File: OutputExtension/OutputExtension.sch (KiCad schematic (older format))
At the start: 18 parts, among them P1 CONN_01X04, P2 CONN_01X04, P3 CONN_01X04, P4 CONN_01X08, P5 CONN_01X08, U1 PCF8574

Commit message: Output extension looks good. Diodes still missing
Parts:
- added JP1: A0, Connector_PinHeader_2.54mm:PinHeader_1x03_P2.54mm_Vertical, symbol Device:Jumper_NC_Dual
- added JP2: A1, Connector_PinHeader_2.54mm:PinHeader_1x03_P2.54mm_Vertical, symbol Device:Jumper_NC_Dual
- added JP3: A2, Connector_PinHeader_2.54mm:PinHeader_1x03_P2.54mm_Vertical, symbol Device:Jumper_NC_Dual
- C1, C2: value 100n -> 1u; footprint Capacitors_ThroughHole:C_Disc_D12_P7.75 -> Capacitor_SMD:C_0805_2012Metric; symbol C -> OutputExtension-rescue:C-OutputExtension-rescue
- C3: value 330n -> 1u; footprint Capacitors_SMD:C_0805_HandSoldering -> Capacitor_SMD:C_0805_2012Metric; symbol C -> OutputExtension-rescue:C-OutputExtension-rescue
- C4: value 100n -> 1u; footprint Capacitors_SMD:C_0805_HandSoldering -> Capacitor_SMD:C_0805_2012Metric; symbol C -> OutputExtension-rescue:C-OutputExtension-rescue
- C5, C6: symbol CP -> OutputExtension-rescue:CP-OutputExtension-rescue
- D1, D2: footprint LEDs:LED-0805 -> LED_SMD:LED_0805_2012Metric; symbol LED -> OutputExtension-rescue:LED-OutputExtension-rescue
- F1, F2: symbol FUSE -> OutputExtension-rescue:FUSE-OutputExtension-rescue
- P1: footprint Pin_Headers:Pin_Header_Straight_1x04 -> Connector_PinHeader_2.54mm:PinHeader_1x04_P2.54mm_Vertical; symbol CONN_01X04 -> OutputExtension-rescue:CONN_01X04-OutputExtension-rescue
- P2: renamed from P3; footprint Pin_Headers:Pin_Header_Straight_1x04 -> Connector_PinHeader_2.54mm:PinHeader_1x04_P2.54mm_Vertical; symbol CONN_01X04 -> OutputExtension-rescue:CONN_01X04-OutputExtension-rescue
- P3: renamed from P2; footprint my_foots:HT396_4 -> myStuff:HT396_4; symbol CONN_01X04 -> OutputExtension-rescue:CONN_01X04-OutputExtension-rescue
- P4, P5: footprint my_foots:HT396_8 -> myStuff:HT396_8; symbol CONN_01X08 -> OutputExtension-rescue:CONN_01X08-OutputExtension-rescue
- R1, R2: symbol R -> OutputExtension-rescue:R-OutputExtension-rescue
- U1: symbol PCA9534 -> OutputExtension-rescue:PCA9534-OutputExtension-rescue
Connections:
- net +5V: now also JP1.3, JP2.3, JP3.3
- net GND: now also JP1.1, JP2.1, JP3.1; no longer U1.1 (A0), U1.2 (A1), U1.3 (A2)
- net powerChannel0/Drain renamed powerChannel0/DRAIN
- net powerChannel1/Drain renamed powerChannel1/DRAIN
- net powerChannel2/Drain renamed powerChannel2/DRAIN
- net powerChannel3/Drain renamed powerChannel3/DRAIN
- net powerChannel4/Drain renamed powerChannel4/DRAIN
- net powerChannel5/Drain renamed powerChannel5/DRAIN
- net powerChannel6/Drain renamed powerChannel6/DRAIN
- net powerChannel7/Drain renamed powerChannel7/DRAIN
- new net A0: JP1.2, U1.1 (A0)
- new net A1: JP2.2, U1.2 (A1)
- new net A2: JP3.2, U1.3 (A2)
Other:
- moved on the sheet: C1, C2, C4, P1, P2

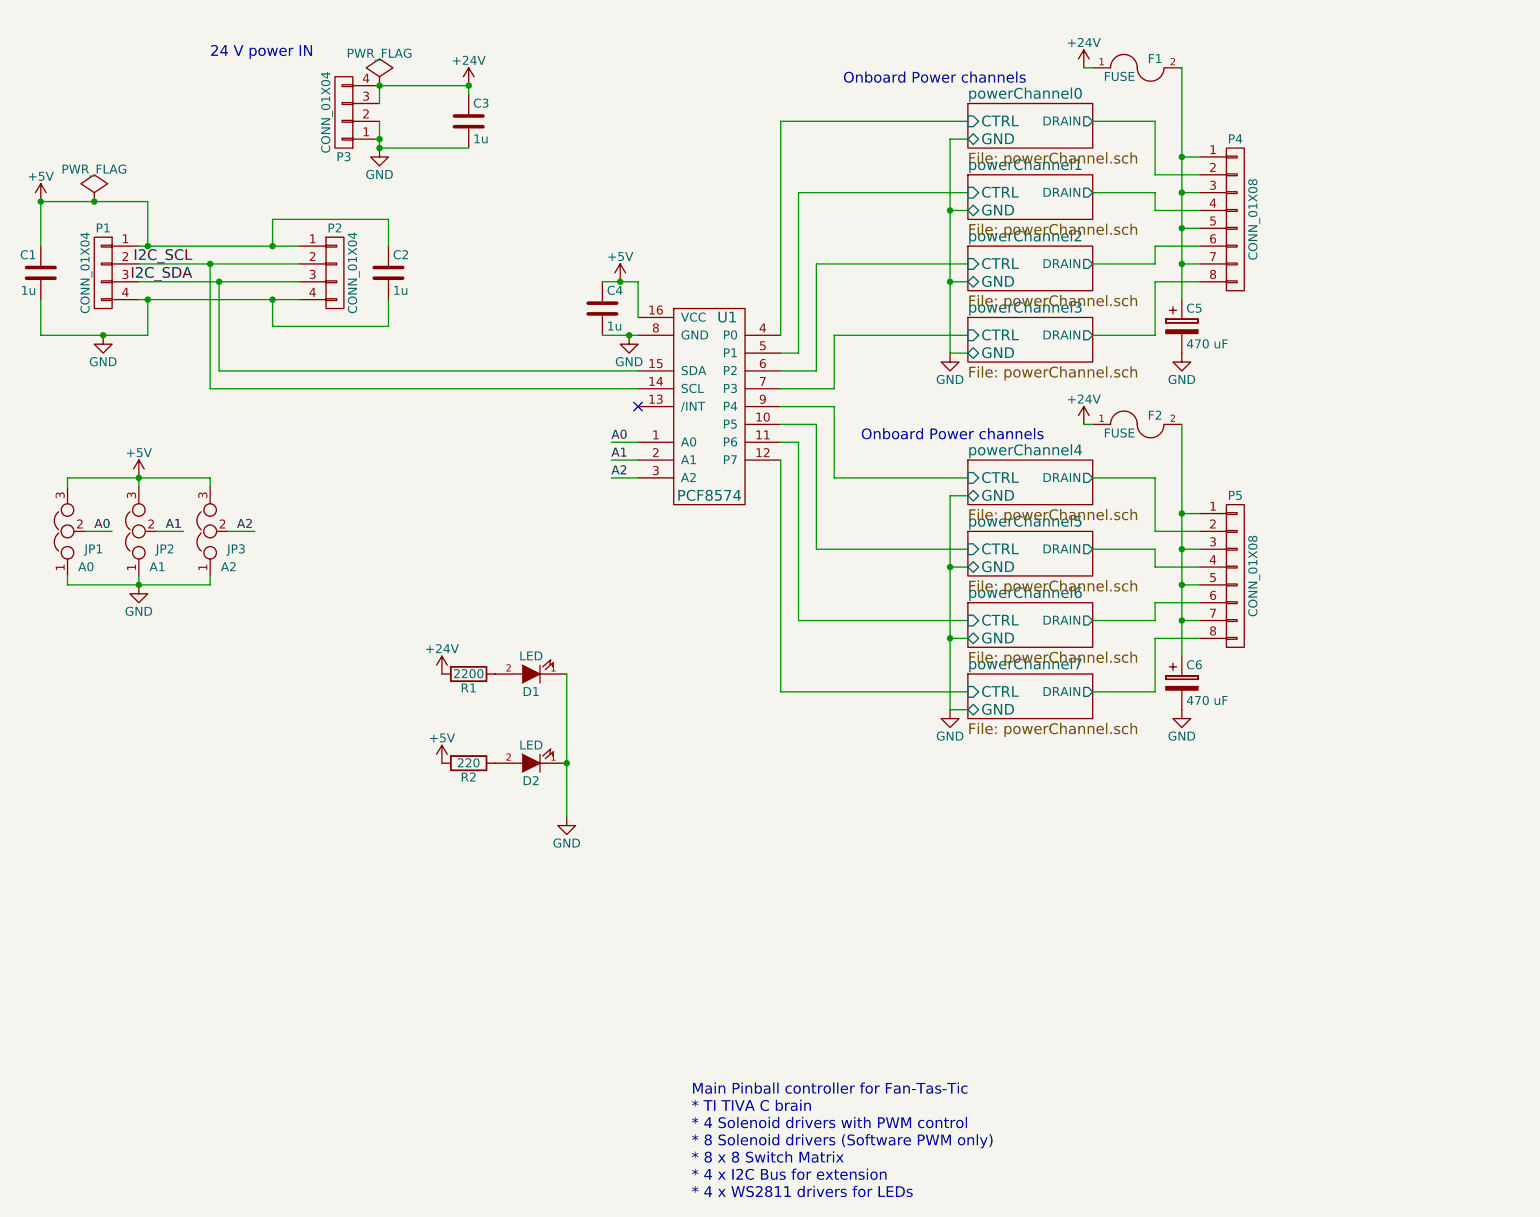
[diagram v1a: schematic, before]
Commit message: Add diodes
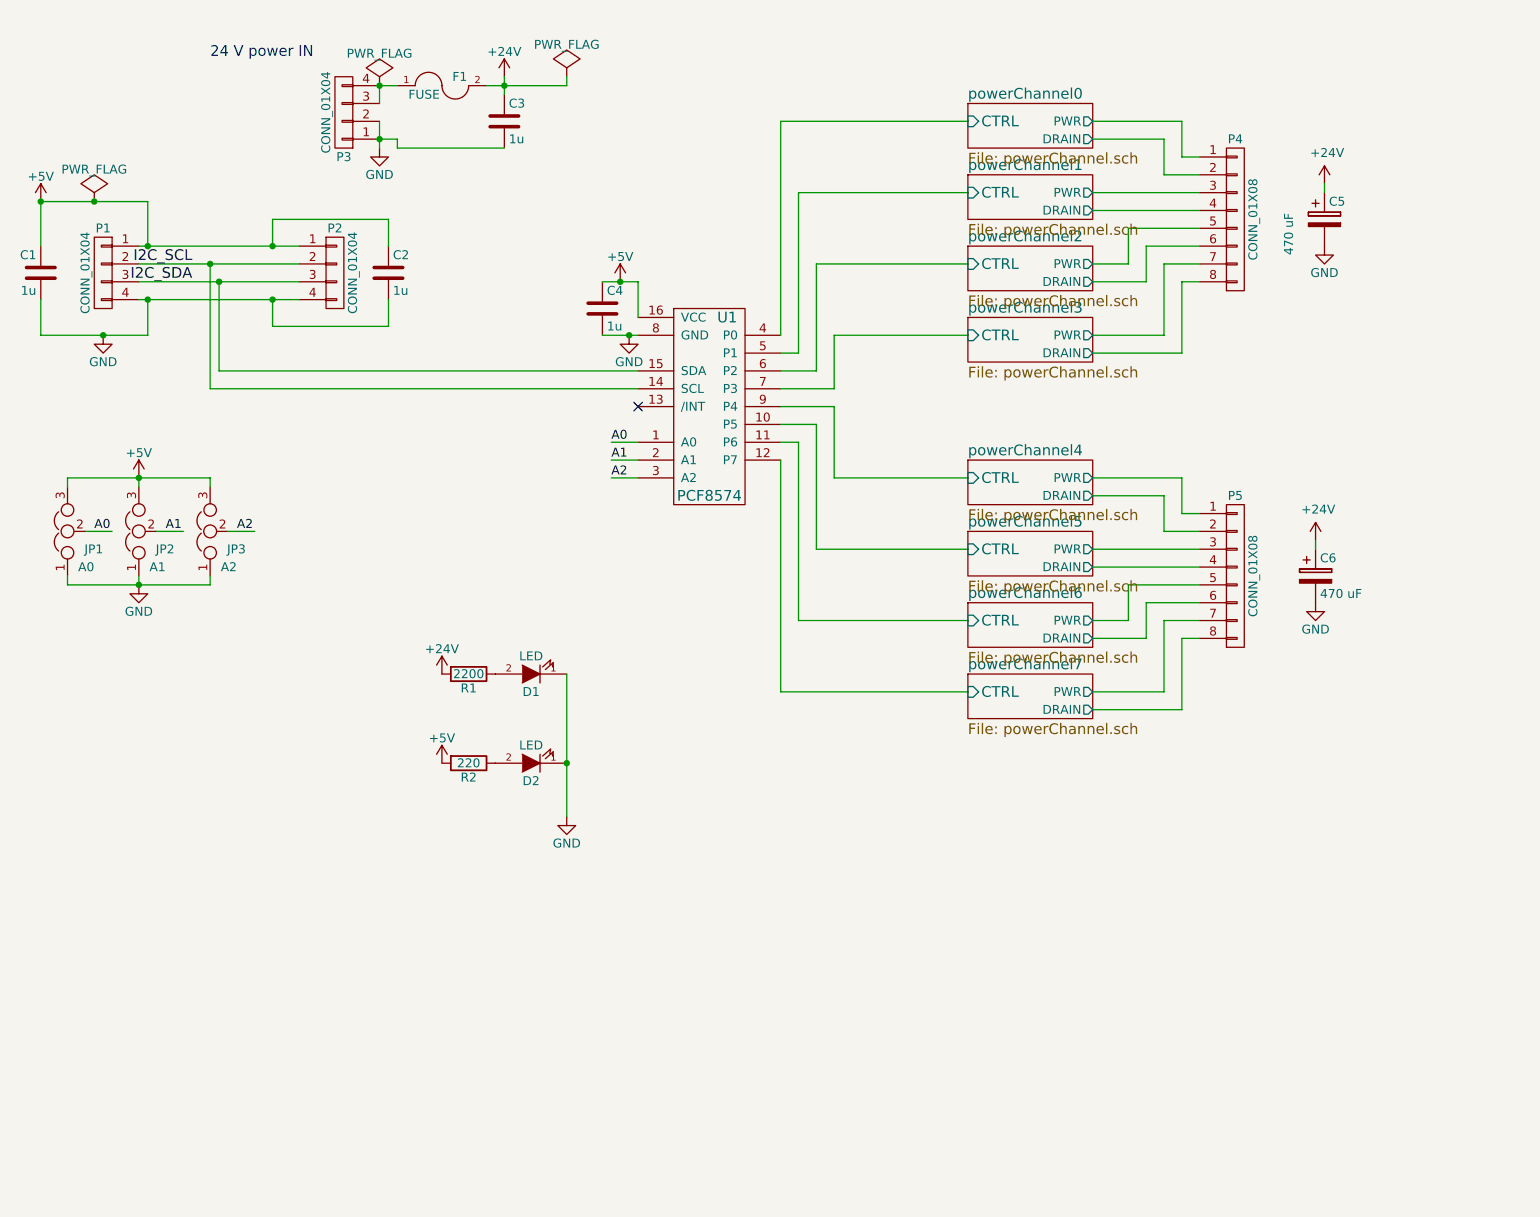
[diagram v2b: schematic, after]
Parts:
- removed F2: FUSE, Fuse_Holders_and_Fuses:Fuseholder5x20_horiz_open_lateral_Type-II, symbol OutputExtension-rescue:FUSE-OutputExtension-rescue
- R1, R2: footprint Resistors_SMD:R_0805_HandSoldering -> Resistor_SMD:R_0805_2012Metric
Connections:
- net +24V: now also C5.1, C6.1, F1.2; no longer F1.1, P3.3 (P3), P3.4 (P4)
- new net: F1.1, P3.3 (P3), P3.4 (P4)
- new net powerChannel0/PWR: P4.1 (P1)
- new net powerChannel1/PWR: P4.3 (P3)
- new net powerChannel2/PWR: P4.5 (P5)
- new net powerChannel3/PWR: P4.7 (P7)
- new net powerChannel4/PWR: P5.1 (P1)
- new net powerChannel5/PWR: P5.3 (P3)
- new net powerChannel6/PWR: P5.5 (P5)
- new net powerChannel7/PWR: P5.7 (P7)
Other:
- note removed: "Main Pinball controller for Fan-Tas-Tic\n* TI TIVA C brain\n* 4 Solenoid drivers with PWM control\n* 8 Solenoid drivers (Software PWM only)\n* 8 x 8 Switch Matrix\n* 4 x I2C Bus for extension\n* 4 x WS2811 drivers for LEDs\n"
- note removed: "Onboard Power channels"
- moved on the sheet: C3, C5, C6, F1

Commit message: Output extension ready for fab
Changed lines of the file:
@@
 $EndComp
 $Sheet
-S 6150 1150 700  250
+S 5950 1150 700  250
 U 568473CE
 F0 "powerChannel0" 60
 F1 "powerChannel.sch" 60
-F2 "CTRL" I L 6150 1250 60
-F3 "DRAIN" O R 6850 1350 50
-F4 "PWR" O R 6850 1250 50
+F2 "CTRL" I L 5950 1250 60
+F3 "DRAIN" O R 6650 1350 50
+F4 "PWR" O R 6650 1250 50
 $EndSheet
 $Comp
@@
 	7350 1450 7450 1450
 Wire Wire Line
-	5200 1650 6150 1650
-Wire Wire Line
-	5400 2450 6150 2450
-Wire Wire Line
-	5100 1250 6150 1250
-Wire Wire Line
-	5300 2050 6150 2050
+	5200 1650 5950 1650
+Wire Wire Line
+	5400 2450 5950 2450
+Wire Wire Line
+	5100 1250 5950 1250
+Wire Wire Line
+	5300 2050 5950 2050
 Wire Wire Line
 	7350 3450 7450 3450
 Wire Wire Line
-	5300 3650 6150 3650
-Wire Wire Line
-	5100 4450 6150 4450
-Wire Wire Line
-	5400 3250 6150 3250
-Wire Wire Line
-	5200 4050 6150 4050
+	5300 3650 5950 3650
+Wire Wire Line
+	5100 4450 5950 4450
+Wire Wire Line
+	5400 3250 5950 3250
+Wire Wire Line
+	5200 4050 5950 4050
 Wire Wire Line
 	5100 2450 5100 1250
@@
 	1950 2150 2400 2150
 $Sheet
-S 6150 2350 700  250
+S 5950 2350 700  250
 U 5BFA64DD
 F0 "powerChannel3" 60
 F1 "powerChannel.sch" 60
-F2 "CTRL" I L 6150 2450 60
-F3 "DRAIN" O R 6850 2550 50
-F4 "PWR" O R 6850 2450 50
+F2 "CTRL" I L 5950 2450 60
+F3 "DRAIN" O R 6650 2550 50
+F4 "PWR" O R 6650 2450 50
 $EndSheet
 $Sheet
-S 6150 3150 700  250
+S 5950 3150 700  250
 U 5BFACA74
 F0 "powerChannel4" 60
 F1 "powerChannel.sch" 60
-F2 "CTRL" I L 6150 3250 60
-F3 "DRAIN" O R 6850 3350 50
-F4 "PWR" O R 6850 3250 50
+F2 "CTRL" I L 5950 3250 60
+F3 "DRAIN" O R 6650 3350 50
+F4 "PWR" O R 6650 3250 50
 $EndSheet
 $Sheet
-S 6150 3550 700  250
+S 5950 3550 700  250
 U 5BFACA79
 F0 "powerChannel5" 60
 F1 "powerChannel.sch" 60
-F2 "CTRL" I L 6150 3650 60
-F3 "DRAIN" O R 6850 3750 50
-F4 "PWR" O R 6850 3650 50
+F2 "CTRL" I L 5950 3650 60
+F3 "DRAIN" O R 6650 3750 50
+F4 "PWR" O R 6650 3650 50
 $EndSheet
 $Sheet
-S 6150 4350 700  250
+S 5950 4350 700  250
 U 5BFACA83
 F0 "powerChannel7" 60
 F1 "powerChannel.sch" 60
-F2 "CTRL" I L 6150 4450 60
-F3 "DRAIN" O R 6850 4550 50
-F4 "PWR" O R 6850 4450 50
+F2 "CTRL" I L 5950 4450 60
+F3 "DRAIN" O R 6650 4550 50
+F4 "PWR" O R 6650 4450 50
 $EndSheet
 Wire Wire Line
-	6850 1750 7450 1750
+	6650 1750 7450 1750
 Wire Wire Line
 	7150 1950 7150 2150
 Wire Wire Line
-	7150 2150 6850 2150
+	7150 2150 6650 2150
 Wire Wire Line
 	7150 1950 7450 1950
 Wire Wire Line
-	6850 3750 7450 3750
+	6650 3750 7450 3750
 Wire Wire Line
 	7150 3950 7150 4150
 Wire Wire Line
-	7150 4150 6850 4150
+	7150 4150 6650 4150
 Wire Wire Line
 	7150 3950 7450 3950
@@
 	8100 3600 8100 3650
 Wire Wire Line
-	6850 3250 7350 3250
+	6650 3250 7350 3250
 Wire Wire Line
 	7350 3250 7350 3450
 Wire Wire Line
-	6850 1250 7350 1250
+	6650 1250 7350 1250
 Wire Wire Line
 	7350 1250 7350 1450
@@
 	8150 1650 8150 1600
 $Sheet
-S 6150 1550 700  250
+S 5950 1550 700  250
 U 5BF99CAF
 F0 "powerChannel1" 60
 F1 "powerChannel.sch" 60
-F2 "CTRL" I L 6150 1650 60
-F3 "DRAIN" O R 6850 1750 50
-F4 "PWR" O R 6850 1650 50
+F2 "CTRL" I L 5950 1650 60
+F3 "DRAIN" O R 6650 1750 50
+F4 "PWR" O R 6650 1650 50
 $EndSheet
 Wire Wire Line
@@
 	2950 1400 3550 1400
 Wire Wire Line
-	6850 1650 7450 1650
+	6650 1650 7450 1650
 $Sheet
-S 6150 1950 700  250
+S 5950 1950 700  250
 U 5BFA00DD
 F0 "powerChannel2" 60
 F1 "powerChannel.sch" 60
-F2 "CTRL" I L 6150 2050 60
-F3 "DRAIN" O R 6850 2150 50
-F4 "PWR" O R 6850 2050 50
+F2 "CTRL" I L 5950 2050 60
+F3 "DRAIN" O R 6650 2150 50
+F4 "PWR" O R 6650 2050 50
 $EndSheet
 Wire Wire Line
 	7050 1850 7050 2050
 Wire Wire Line
-	7050 2050 6850 2050
+	7050 2050 6650 2050
 Wire Wire Line
 	7050 1850 7450 1850
@@
 	7250 2050 7250 2450
 Wire Wire Line
-	7250 2450 6850 2450
+	7250 2450 6650 2450
 Wire Wire Line
 	7350 2550 7350 2150
@@
 	7350 2150 7450 2150
 Wire Wire Line
-	6850 2550 7350 2550
+	6650 2550 7350 2550
 Wire Wire Line
 	7250 1350 7250 1550
 Wire Wire Line
-	6850 1350 7250 1350
+	6650 1350 7250 1350
 Wire Wire Line
 	7250 1550 7450 1550
@@
 $EndComp
 Wire Wire Line
-	6850 3650 7450 3650
+	6650 3650 7450 3650
 Wire Wire Line
 	7250 3350 7250 3550
 Wire Wire Line
-	6850 3350 7250 3350
+	6650 3350 7250 3350
 Wire Wire Line
 	7250 3550 7450 3550
 $Sheet
-S 6150 3950 700  250
+S 5950 3950 700  250
 U 5BFACA7E
 F0 "powerChannel6" 60
 F1 "powerChannel.sch" 60
-F2 "CTRL" I L 6150 4050 60
-F3 "DRAIN" O R 6850 4150 50
-F4 "PWR" O R 6850 4050 50
+F2 "CTRL" I L 5950 4050 60
+F3 "DRAIN" O R 6650 4150 50
+F4 "PWR" O R 6650 4050 50
 $EndSheet
 Wire Wire Line
 	7050 3850 7050 4050
 Wire Wire Line
-	7050 4050 6850 4050
+	7050 4050 6650 4050
 Wire Wire Line
 	7050 3850 7450 3850
@@
 	7250 4050 7250 4450
 Wire Wire Line
-	7250 4450 6850 4450
+	7250 4450 6650 4450
 Wire Wire Line
 	7350 4550 7350 4150
@@
 	7350 4150 7450 4150
 Wire Wire Line
-	6850 4550 7350 4550
+	6650 4550 7350 4550
 $Comp
 L OutputExtension-rescue:PWR_FLAG-OutputExtension-rescue #FLG0101

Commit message: Fabbed version
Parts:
- added F2: FUSE, myStuff:littlefuse_154_smd, symbol OutputExtension-rescue:FUSE-OutputExtension-rescue
- F1: footprint Fuse_Holders_and_Fuses:Fuseholder5x20_horiz_open_lateral_Type-II -> myStuff:LBL_FUSE
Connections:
- net +24V: now also F2.2
- net at F1.1, P3.3 (P3), P3.4 (P4): now also F2.1
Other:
- moved on the sheet: F1
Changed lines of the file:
@@
 L OutputExtension-rescue:FUSE-OutputExtension-rescue F1
 U 1 1 568473CC
-P 3200 1050
-F 0 "F1" H 3300 1100 50  0000 C CNN
-F 1 "FUSE" H 3100 1000 50  0000 C CNN
-F 2 "Fuse_Holders_and_Fuses:Fuseholder5x20_horiz_open_lateral_Type-II" H 3200 1050 50  0001 C CNN
-F 3 "" H 3200 1050 50  0000 C CNN
-	1    3200 1050
+P 3200 950
+F 0 "F1" H 3300 1000 50  0000 C CNN
+F 1 "FUSE" H 3100 900 50  0000 C CNN
+F 2 "myStuff:LBL_FUSE" H 3200 950 50  0001 C CNN
+F 3 "" H 3200 950 50  0000 C CNN
+	1    3200 950
 	1    0    0    -1
 $EndComp
@@
 P 2850 1050
 F 0 "#FLG02" H 2850 1145 50  0001 C CNN
-F 1 "PWR_FLAG" H 2850 1230 50  0000 C CNN
+F 1 "PWR_FLAG" H 2650 1400 50  0000 C CNN
 F 2 "" H 2850 1050 50  0000 C CNN
 F 3 "" H 2850 1050 50  0000 C CNN
@@
 Wire Wire Line
 	3900 1050 3550 1050
+$Comp
+L OutputExtension-rescue:FUSE-OutputExtension-rescue F2
+U 1 1 5BED216F
+P 3200 1150
+F 0 "F2" H 3300 1200 50  0000 C CNN
+F 1 "FUSE" H 3100 1100 50  0000 C CNN
+F 2 "myStuff:littlefuse_154_smd" H 3200 1150 50  0001 C CNN
+F 3 "" H 3200 1150 50  0000 C CNN
+	1    3200 1150
+	1    0    0    -1
+$EndComp
+Wire Wire Line
+	2950 1050 2950 950
+Wire Wire Line
+	2950 1050 2950 1150
+Connection ~ 2950 1050
+Wire Wire Line
+	3450 1050 3450 950
+Wire Wire Line
+	3450 1050 3450 1150
+Connection ~ 3450 1050
 $EndSCHEMATC

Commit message: Output extension: chunkier freewheelingdiode
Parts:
- F2: value FUSE -> FUSE_DNP
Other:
- note added: "Rev1: Change freeweeling diode footprint to SMC"
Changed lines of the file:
@@
 encoding utf-8
 Sheet 1 9
-Title ""
-Date ""
-Rev ""
-Comp ""
+Title "Fan-Tas-Tic output extension"
+Date "2018-12-16"
+Rev "1"
+Comp "M. Betz"
 Comment1 ""
 Comment2 ""
 Comment3 ""
-Comment4 ""
+Comment4 "8 clunky outputs to drive your solenoids"
 $EndDescr
 $Comp
@@
 P 3200 1150
 F 0 "F2" H 3300 1200 50  0000 C CNN
-F 1 "FUSE" H 3100 1100 50  0000 C CNN
+F 1 "FUSE_DNP" H 3150 1000 50  0000 C CNN
 F 2 "myStuff:littlefuse_154_smd" H 3200 1150 50  0001 C CNN
 F 3 "" H 3200 1150 50  0000 C CNN
@@
 	3450 1050 3450 1150
 Connection ~ 3450 1050
+Text Notes 7000 6800 0    50   ~ 0
+Rev1: Change freeweeling diode footprint to SMC
 $EndSCHEMATC
